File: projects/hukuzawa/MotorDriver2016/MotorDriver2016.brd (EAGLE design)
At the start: 116.8 x 99.1 mm, 54 parts, among them IC1 PIC16F648, IC2 TLP521, IC3 TLP521, J3 3PIN(L), J4 3PIN(L)

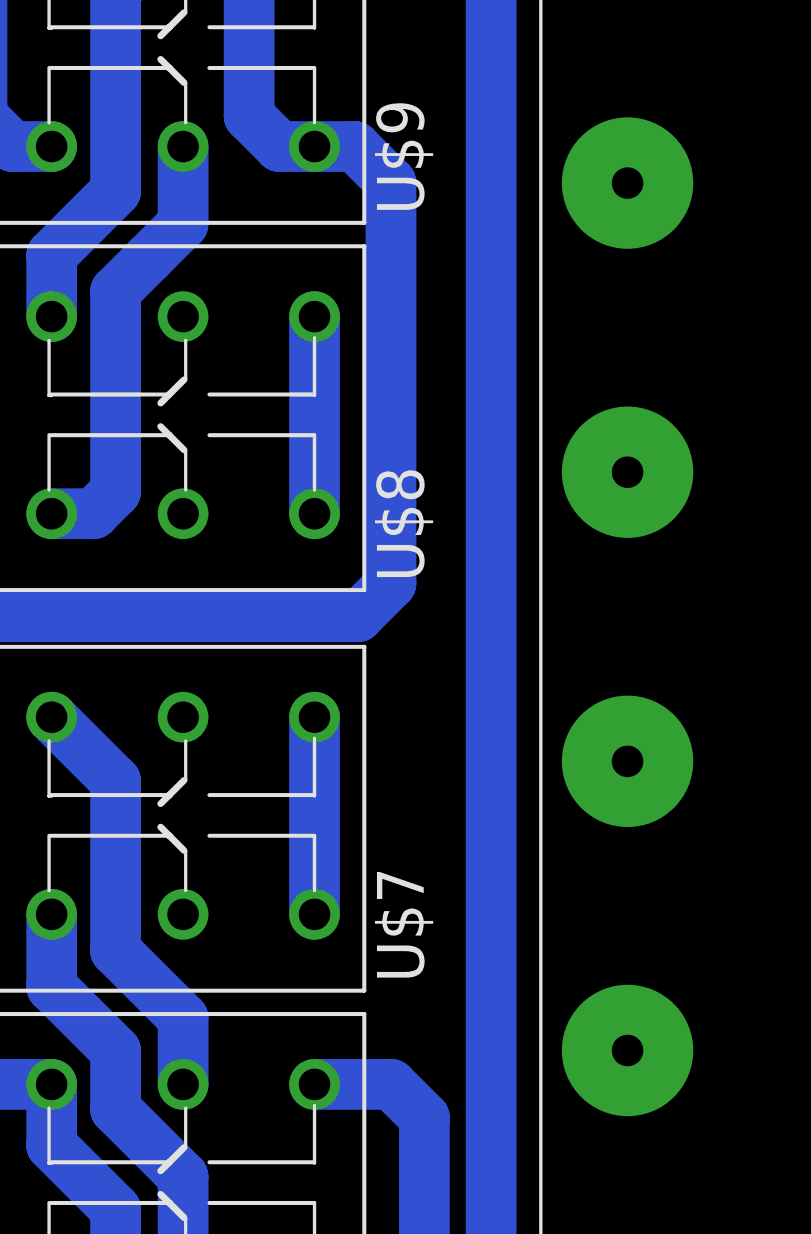
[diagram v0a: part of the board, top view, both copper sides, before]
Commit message: 旧モータードライバ修正
ハッチングデータ修正
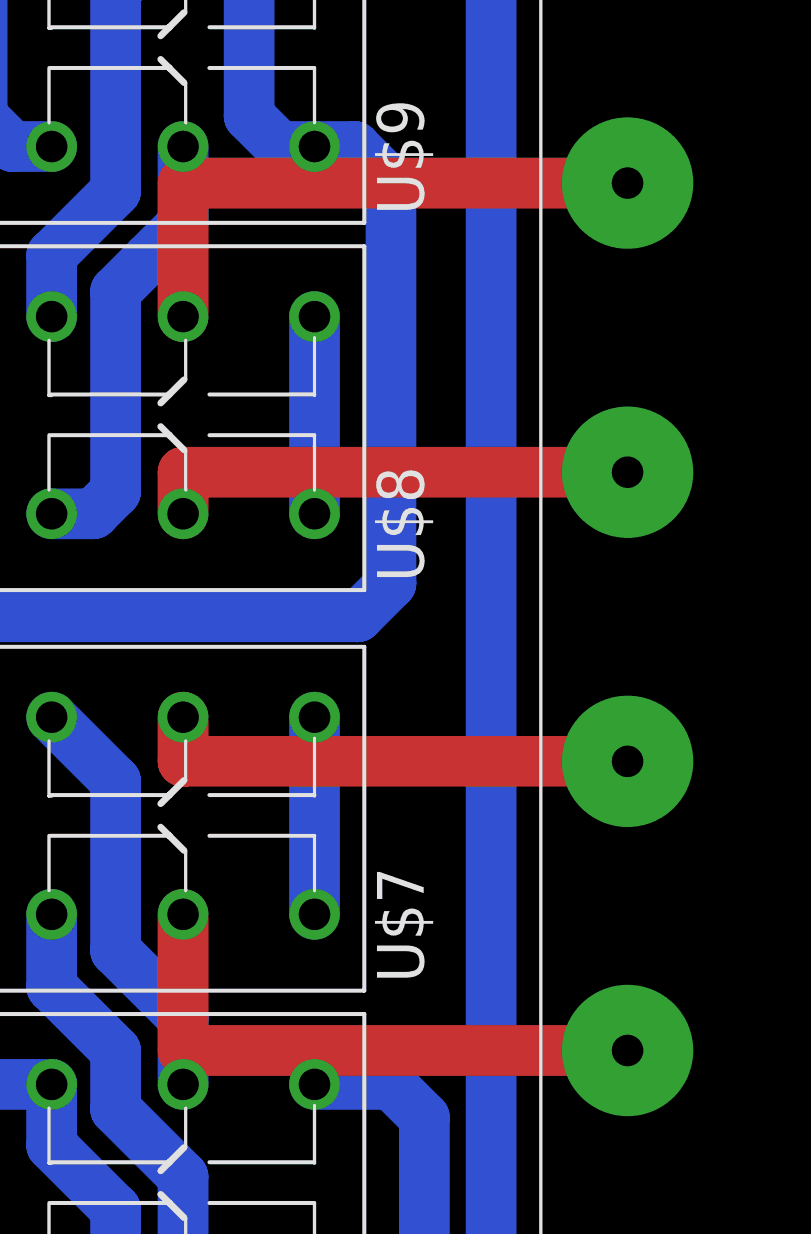
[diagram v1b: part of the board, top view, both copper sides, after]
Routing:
- net OUTB-: track 0.00 -> 22.1 mm
- net OUTA+: track 0.00 -> 22.0 mm
- net OUTB+: track 0.00 -> 18.6 mm
- net OUTA-: track 0.00 -> 18.5 mm
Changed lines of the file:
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@@
 <layer number="121" name="_tplace" color="14" fill="1" visible="no" active="yes"/>
 <layer number="122" name="_bplace" color="14" fill="1" visible="no" active="yes"/>
-<layer number="150" name="hatching" color="13" fill="1" visible="yes" active="yes"/>
+<layer number="150" name="hatching" color="13" fill="3" visible="yes" active="yes"/>
 <layer number="250" name="Descript" color="3" fill="1" visible="no" active="no"/>
 <layer number="251" name="SMDround" color="12" fill="11" visible="no" active="no"/>
@@
 <wire x1="116.84" y1="99.06" x2="0" y2="99.06" width="0" layer="20"/>
 <wire x1="0" y1="99.06" x2="0" y2="0" width="0" layer="20"/>
-<wire x1="25.4" y1="91.44" x2="25.4" y2="78.74" width="0.4064" layer="150"/>
-<wire x1="59.69" y1="7.62" x2="62.23" y2="5.08" width="0.4064" layer="150"/>
-<wire x1="62.23" y1="5.08" x2="100.33" y2="5.08" width="0.4064" layer="150"/>
 <wire x1="100.33" y1="93.98" x2="27.94" y2="93.98" width="0.4064" layer="150"/>
-<wire x1="27.94" y1="93.98" x2="25.4" y2="91.44" width="0.4064" layer="150"/>
-<wire x1="105.41" y1="71.12" x2="107.95" y2="71.12" width="0.4064" layer="150"/>
-<wire x1="107.95" y1="71.12" x2="110.49" y2="68.58" width="0.4064" layer="150"/>
-<wire x1="110.49" y1="68.58" x2="110.49" y2="30.48" width="0.4064" layer="150"/>
-<wire x1="110.49" y1="30.48" x2="107.95" y2="27.94" width="0.4064" layer="150"/>
-<wire x1="107.95" y1="27.94" x2="105.41" y2="27.94" width="0.4064" layer="150"/>
-<wire x1="25.4" y1="78.74" x2="27.94" y2="76.2" width="0.4064" layer="150"/>
-<wire x1="72.39" y1="72.39" x2="74.93" y2="69.85" width="0.4064" layer="150"/>
-<wire x1="100.33" y1="93.98" x2="102.87" y2="91.44" width="0.4064" layer="150"/>
-<wire x1="102.87" y1="91.44" x2="102.87" y2="73.66" width="0.4064" layer="150"/>
-<wire x1="102.87" y1="73.66" x2="105.41" y2="71.12" width="0.4064" layer="150"/>
-<wire x1="100.33" y1="5.08" x2="102.87" y2="7.62" width="0.4064" layer="150"/>
-<wire x1="102.87" y1="7.62" x2="102.87" y2="25.4" width="0.4064" layer="150"/>
-<wire x1="102.87" y1="25.4" x2="105.41" y2="27.94" width="0.4064" layer="150"/>
-<wire x1="59.69" y1="7.62" x2="59.69" y2="17.78" width="0.4064" layer="150"/>
-<wire x1="59.69" y1="17.78" x2="62.23" y2="20.32" width="0.4064" layer="150"/>
-<wire x1="62.23" y1="20.32" x2="72.39" y2="20.32" width="0.4064" layer="150"/>
-<wire x1="72.39" y1="20.32" x2="74.93" y2="22.86" width="0.4064" layer="150"/>
-<wire x1="74.93" y1="22.86" x2="74.93" y2="69.85" width="0.4064" layer="150"/>
-<wire x1="27.94" y1="76.2" x2="58.42" y2="76.2" width="0.4064" layer="150"/>
-<wire x1="58.42" y1="76.2" x2="62.23" y2="72.39" width="0.4064" layer="150"/>
-<wire x1="62.23" y1="72.39" x2="72.39" y2="72.39" width="0.4064" layer="150"/>
+<polygon width="0.4064" layer="150">
+<vertex x="27.94" y="93.98"/>
+<vertex x="25.4" y="91.44"/>
+<vertex x="25.4" y="78.74"/>
+<vertex x="27.94" y="76.2"/>
+<vertex x="58.42" y="76.2"/>
+<vertex x="62.23" y="72.39"/>
+<vertex x="72.39" y="72.39"/>
+<vertex x="74.93" y="69.85"/>
+<vertex x="74.93" y="22.86"/>
+<vertex x="72.39" y="20.32"/>
+<vertex x="62.23" y="20.32"/>
+<vertex x="59.69" y="17.78"/>
+<vertex x="59.69" y="7.62"/>
+<vertex x="62.23" y="5.08"/>
+<vertex x="100.33" y="5.08"/>
+<vertex x="102.87" y="7.62"/>
+<vertex x="102.87" y="25.4"/>
+<vertex x="105.41" y="27.94"/>
+<vertex x="107.95" y="27.94"/>
+<vertex x="110.49" y="30.48"/>
+<vertex x="110.49" y="68.58"/>
+<vertex x="107.95" y="71.12"/>
+<vertex x="105.41" y="71.12"/>
+<vertex x="102.87" y="73.66"/>
+<vertex x="102.87" y="91.44"/>
+<vertex x="100.33" y="93.98"/>
+</polygon>
 </plain>
 <attributes>
@@
 <contactref element="U$8" pad="3"/>
 <contactref element="U$2" pad="P2"/>
-<wire x1="88.61" y1="53.45" x2="105.52" y2="55.03" width="0" layer="19" extent="1-1"/>
+<wire x1="105.52" y1="55.03" x2="88.61" y2="55.03" width="1.9304" layer="1"/>
+<wire x1="88.61" y1="55.03" x2="88.61" y2="53.45" width="1.9304" layer="1"/>
 </signal>
 <signal name="OUTA+">
 <contactref element="U$8" pad="6"/>
 <contactref element="U$2" pad="P1"/>
-<wire x1="88.61" y1="60.95" x2="105.52" y2="66.03" width="0" layer="19" extent="1-1"/>
+<wire x1="105.52" y1="66.03" x2="88.61" y2="66.03" width="1.9304" layer="1"/>
+<wire x1="88.61" y1="66.03" x2="88.61" y2="60.95" width="1.9304" layer="1"/>
 </signal>
 <signal name="OUTB+">
 <contactref element="U$2" pad="P3"/>
 <contactref element="U$7" pad="6"/>
-<wire x1="88.61" y1="45.71" x2="105.52" y2="44.03" width="0" layer="19" extent="1-1"/>
+<wire x1="105.52" y1="44.03" x2="88.61" y2="44.03" width="1.9304" layer="1"/>
+<wire x1="88.61" y1="44.03" x2="88.61" y2="45.71" width="1.9304" layer="1"/>
 </signal>
 <signal name="OUTB-">
 <contactref element="U$2" pad="P4"/>
 <contactref element="U$7" pad="3"/>
-<wire x1="88.61" y1="38.21" x2="105.52" y2="33.03" width="0" layer="19" extent="1-1"/>
+<wire x1="105.52" y1="33.03" x2="88.61" y2="33.03" width="1.9304" layer="1"/>
+<wire x1="88.61" y1="33.03" x2="88.61" y2="38.21" width="1.9304" layer="1"/>
 </signal>
 </signals>

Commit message: 旧モータードライバ更新
使用抵抗の値を変更
イメージファイルにエクスポート
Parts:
- R13, R14: value 510 -> 1k
- R2, R3, R4, R5, R6, R7: value 10k -> 330
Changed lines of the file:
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@@
 <element name="R10" library="rcl" package="R3216W" value="10k" x="54.61" y="36.83" rot="MR180"/>
 <element name="R11" library="rcl" package="R3216W" value="10k" x="54.61" y="22.86" rot="MR180"/>
-<element name="R13" library="rcl" package="R3216W" value="510" x="54.61" y="45.72" rot="MR0"/>
+<element name="R13" library="rcl" package="R3216W" value="1k" x="54.61" y="45.72" rot="MR0"/>
 <element name="TR1" library="My_transistor" package="TO92BCE" value="2SC2001" x="60.96" y="24.13" rot="R270"/>
 <element name="TR2" library="My_transistor" package="TO92BCE" value="2SC2001" x="60.96" y="38.1" rot="R270"/>
@@
 <element name="R1" library="rcl" package="R3216W" value="2k" x="10.16" y="27.94" rot="MR270"/>
 <element name="IC1" library="FP-21T for MITS" package="DIL18" value="PIC16F648" x="19.05" y="17.78" rot="R270"/>
-<element name="R2" library="rcl" package="R3216W" value="10k" x="35.56" y="58.42" rot="MR180"/>
-<element name="R3" library="rcl" package="R3216W" value="10k" x="35.56" y="63.5" rot="MR180"/>
-<element name="R4" library="rcl" package="R3216W" value="10k" x="35.56" y="68.58" rot="MR180"/>
-<element name="R5" library="rcl" package="R3216W" value="10k" x="35.56" y="16.51" rot="MR180"/>
-<element name="R6" library="rcl" package="R3216W" value="10k" x="35.56" y="21.59" rot="MR180"/>
-<element name="R7" library="rcl" package="R3216W" value="10k" x="35.56" y="26.67" rot="MR180"/>
+<element name="R2" library="rcl" package="R3216W" value="330" x="35.56" y="58.42" rot="MR180"/>
+<element name="R3" library="rcl" package="R3216W" value="330" x="35.56" y="63.5" rot="MR180"/>
+<element name="R4" library="rcl" package="R3216W" value="330" x="35.56" y="68.58" rot="MR180"/>
+<element name="R5" library="rcl" package="R3216W" value="330" x="35.56" y="16.51" rot="MR180"/>
+<element name="R6" library="rcl" package="R3216W" value="330" x="35.56" y="21.59" rot="MR180"/>
+<element name="R7" library="rcl" package="R3216W" value="330" x="35.56" y="26.67" rot="MR180"/>
 <element name="IC2" library="FP-21T for MITS" package="DIL16" value="TLP521" x="43.18" y="59.69" rot="R270"/>
 <element name="IC3" library="FP-21T for MITS" package="DIL16" value="TLP521" x="43.18" y="17.78" rot="R270"/>
@@
 <element name="U$3" library="My_rcl" package="C-6MM" value="C-ELEC" x="16.51" y="62.23" rot="R180"/>
 <element name="C1" library="My_rcl" package="C-2.54" value="" x="16.51" y="57.15"/>
-<element name="R14" library="rcl" package="R3216W" value="510" x="55.88" y="12.7" rot="MR90"/>
+<element name="R14" library="rcl" package="R3216W" value="1k" x="55.88" y="12.7" rot="MR90"/>
 <element name="U$5" library="FET_kai" package="TO220BV" value="N-MOS" x="63.5" y="12.7" rot="R270"/>
 <element name="U$10" library="FET_kai" package="TO220BV" value="N-MOS" x="69.85" y="12.7" rot="R270"/>
